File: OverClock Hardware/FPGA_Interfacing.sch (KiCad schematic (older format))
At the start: 17 parts

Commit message: Completed Schematic and ran ERC
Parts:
- gave numbers to parts that had none: 17
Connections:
- no-connect marks 8 -> 10
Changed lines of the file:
@@
 $EndDescr
 $Comp
-L Maxted_Libs:10M02SCE144 U?
+L Maxted_Libs:10M02SCE144 U3
 U 2 1 5C67791D
 P 4350 3300
-F 0 "U?" H 4425 2678 50  0000 C CNN
+F 0 "U3" H 4425 2678 50  0000 C CNN
 F 1 "10M02SCE144" H 4425 2587 50  0000 C CNN
 F 2 "Maxted Libs:QFP-144_EPAD_20x20_Pitch0.5mm" H 5350 4100 50  0001 C CNN
@@
 +3V
 $Comp
-L Device:R_Small R?
+L Device:R_Small R9
 U 1 1 5C68AD28
 P 5900 3700
-F 0 "R?" H 5959 3746 50  0000 L CNN
+F 0 "R9" H 5959 3746 50  0000 L CNN
 F 1 "1K" H 5959 3655 50  0000 L CNN
 F 2 "" H 5900 3700 50  0001 C CNN
@@
 $EndComp
 $Comp
-L power:GND #PWR?
+L power:GND #PWR08
 U 1 1 5C68ADAE
 P 5900 3800
-F 0 "#PWR?" H 5900 3550 50  0001 C CNN
+F 0 "#PWR08" H 5900 3550 50  0001 C CNN
 F 1 "GND" H 5905 3627 50  0000 C CNN
 F 2 "" H 5900 3800 50  0001 C CNN
@@
 	6150 3150 6150 3600
 $Comp
-L Device:R_Small R?
+L Device:R_Small R10
 U 1 1 5C692EE8
 P 6150 3700
-F 0 "R?" H 6209 3746 50  0000 L CNN
+F 0 "R10" H 6209 3746 50  0000 L CNN
 F 1 "1K" H 6209 3655 50  0000 L CNN
 F 2 "" H 6150 3700 50  0001 C CNN
@@
 $EndComp
 $Comp
-L power:GND #PWR?
+L power:GND #PWR09
 U 1 1 5C692FE7
 P 6150 3800
-F 0 "#PWR?" H 6150 3550 50  0001 C CNN
+F 0 "#PWR09" H 6150 3550 50  0001 C CNN
 F 1 "GND" H 6155 3627 50  0000 C CNN
 F 2 "" H 6150 3800 50  0001 C CNN
@@
 	6000 3250 6000 2900
 $Comp
-L Device:R_Small R?
+L Device:R_Small R3
 U 1 1 5C69923E
 P 6000 2800
-F 0 "R?" H 6059 2846 50  0000 L CNN
+F 0 "R3" H 6059 2846 50  0000 L CNN
 F 1 "1K" H 6059 2755 50  0000 L CNN
 F 2 "" H 6000 2800 50  0001 C CNN
@@
 $EndComp
 $Comp
-L Device:R_Small R?
+L Device:R_Small R4
 U 1 1 5C699292
 P 6300 2800
-F 0 "R?" H 6359 2846 50  0000 L CNN
+F 0 "R4" H 6359 2846 50  0000 L CNN
 F 1 "1K" H 6359 2755 50  0000 L CNN
 F 2 "" H 6300 2800 50  0001 C CNN
@@
 Connection ~ 6000 2700
 $Comp
-L Maxted_Libs:JTAG_HDR J?
+L Maxted_Libs:JTAG_HDR J2
 U 1 1 5C6A069B
 P 6700 3300
-F 0 "J?" H 6900 3650 50  0000 L CNN
+F 0 "J2" H 6900 3650 50  0000 L CNN
 F 1 "JTAG_HDR" H 6900 3500 50  0000 L CNN
 F 2 "Connector_PinHeader_2.54mm:PinHeader_2x05_P2.54mm_Vertical" H 6550 4200 50  0001 C CNN
@@
 $EndComp
 $Comp
-L power:GND #PWR?
+L power:GND #PWR07
 U 1 1 5C6A0707
 P 6850 3750
-F 0 "#PWR?" H 6850 3500 50  0001 C CNN
+F 0 "#PWR07" H 6850 3500 50  0001 C CNN
 F 1 "GND" H 6855 3577 50  0000 C CNN
 F 2 "" H 6850 3750 50  0001 C CNN
@@
 	7050 3700 7050 3200
 $Comp
-L Device:C_Small C?
+L Device:C_Small C23
 U 1 1 5C6B33C4
 P 5350 2550
-F 0 "C?" H 5442 2596 50  0000 L CNN
+F 0 "C23" H 5442 2596 50  0000 L CNN
 F 1 "10nF" H 5442 2505 50  0000 L CNN
 F 2 "" H 5350 2550 50  0001 C CNN
@@
 $EndComp
 $Comp
-L power:GND #PWR?
+L power:GND #PWR06
 U 1 1 5C6B34AA
 P 5700 2650
-F 0 "#PWR?" H 5700 2400 50  0001 C CNN
+F 0 "#PWR06" H 5700 2400 50  0001 C CNN
 F 1 "GND" H 5705 2477 50  0000 C CNN
 F 2 "" H 5700 2650 50  0001 C CNN
@@
 	5350 3150 6150 3150
 $Comp
-L Device:C_Small C?
+L Device:C_Small C24
 U 1 1 5C6CAB44
 P 5700 2550
-F 0 "C?" H 5792 2596 50  0000 L CNN
+F 0 "C24" H 5792 2596 50  0000 L CNN
 F 1 "10nF" H 5792 2505 50  0000 L CNN
 F 2 "" H 5700 2550 50  0001 C CNN
@@
 One decoupling cap per Vcc_IO pin.
 $Comp
-L Connector:Conn_01x03_Female J?
+L Connector:Conn_01x03_Female J3
 U 1 1 5C9FC99B
 P 6600 4850
-F 0 "J?" H 6627 4876 50  0000 L CNN
+F 0 "J3" H 6627 4876 50  0000 L CNN
 F 1 "Conn_01x03_Female" H 6300 5100 50  0000 L CNN
 F 2 "Connector_Harwin:Harwin_M20-89003xx_1x03_P2.54mm_Horizontal" H 6600 4850 50  0001 C CNN
@@
 $EndComp
 $Comp
-L power:GND #PWR?
+L power:GND #PWR010
 U 1 1 5C9FCB4B
 P 6400 4950
-F 0 "#PWR?" H 6400 4700 50  0001 C CNN
+F 0 "#PWR010" H 6400 4700 50  0001 C CNN
 F 1 "GND" H 6405 4777 50  0000 C CNN
 F 2 "" H 6400 4950 50  0001 C CNN
@@
 NoConn ~ 5350 3450
 $Comp
-L Maxted_Libs:Switch_Momentary SW?
+L Maxted_Libs:Switch_Momentary SW1
 U 1 1 5CA00362
 P 1850 5100
-F 0 "SW?" H 1800 5250 50  0000 L CNN
+F 0 "SW1" H 1800 5250 50  0000 L CNN
 F 1 "Switch_Momentary" H 1750 5250 50  0001 L CNN
 F 2 "Maxted Libs:Switch_Momentary" H 1600 4950 50  0001 C CNN
@@
 $EndComp
 $Comp
-L Maxted_Libs:Switch_Momentary SW?
+L Maxted_Libs:Switch_Momentary SW2
 U 1 1 5CA005C3
 P 2300 5100
-F 0 "SW?" H 2250 5250 50  0000 L CNN
+F 0 "SW2" H 2250 5250 50  0000 L CNN
 F 1 "Switch_Momentary" H 2200 5250 50  0001 L CNN
 F 2 "Maxted Libs:Switch_Momentary" H 2050 4950 50  0001 C CNN
@@
 $EndComp
 $Comp
-L Maxted_Libs:Switch_Momentary SW?
+L Maxted_Libs:Switch_Momentary SW3
 U 1 1 5CA009D6
 P 2750 5100
-F 0 "SW?" H 2700 5250 50  0000 L CNN
+F 0 "SW3" H 2700 5250 50  0000 L CNN
 F 1 "Switch_Momentary" H 2650 5250 50  0001 L CNN
 F 2 "Maxted Libs:Switch_Momentary" H 2500 4950 50  0001 C CNN
@@
 $EndComp
 $Comp
-L Maxted_Libs:Switch_Momentary SW?
+L Maxted_Libs:Switch_Momentary SW4
 U 1 1 5CA00DE5
 P 3150 5100
-F 0 "SW?" H 3100 5250 50  0000 L CNN
+F 0 "SW4" H 3100 5250 50  0000 L CNN
 F 1 "Switch_Momentary" H 3050 5250 50  0001 L CNN
 F 2 "Maxted Libs:Switch_Momentary" H 2900 4950 50  0001 C CNN
@@
 	3050 5200 2900 5200
 $Comp
-L power:GND #PWR?
+L power:GND #PWR011
 U 1 1 5CA05B6C
 P 1750 5200
-F 0 "#PWR?" H 1750 4950 50  0001 C CNN
+F 0 "#PWR011" H 1750 4950 50  0001 C CNN
 F 1 "GND" H 1755 5027 50  0000 C CNN
 F 2 "" H 1750 5200 50  0001 C CNN
@@
 	1700 5750 1700 5450
 $Comp
-L Device:R_Small R?
+L Device:R_Small R8
 U 1 1 5CA06FA7
 P 3150 3100
-F 0 "R?" H 3209 3146 50  0000 L CNN
+F 0 "R8" H 3209 3146 50  0000 L CNN
 F 1 "1K" H 3209 3055 50  0000 L CNN
 F 2 "Resistor_SMD:R_0805_2012Metric_Pad1.15x1.40mm_HandSolder" H 3150 3100 50  0001 C CNN
@@
 $EndComp
 $Comp
-L Device:R_Small R?
+L Device:R_Small R7
 U 1 1 5CA0718A
 P 2750 3100
-F 0 "R?" H 2809 3146 50  0000 L CNN
+F 0 "R7" H 2809 3146 50  0000 L CNN
 F 1 "1K" H 2809 3055 50  0000 L CNN
 F 2 "Resistor_SMD:R_0805_2012Metric_Pad1.15x1.40mm_HandSolder" H 2750 3100 50  0001 C CNN
@@
 $EndComp
 $Comp
-L Device:R_Small R?
+L Device:R_Small R6
 U 1 1 5CA081C0
 P 2300 3100
-F 0 "R?" H 2359 3146 50  0000 L CNN
+F 0 "R6" H 2359 3146 50  0000 L CNN
 F 1 "1K" H 2359 3055 50  0000 L CNN
 F 2 "Resistor_SMD:R_0805_2012Metric_Pad1.15x1.40mm_HandSolder" H 2300 3100 50  0001 C CNN
@@
 $EndComp
 $Comp
-L Device:R_Small R?
+L Device:R_Small R5
 U 1 1 5CA09200
 P 1850 3100
-F 0 "R?" H 1909 3146 50  0000 L CNN
+F 0 "R5" H 1909 3146 50  0000 L CNN
 F 1 "1K" H 1909 3055 50  0000 L CNN
 F 2 "Resistor_SMD:R_0805_2012Metric_Pad1.15x1.40mm_HandSolder" H 1850 3100 50  0001 C CNN
@@
 NoConn ~ 3500 3150
 NoConn ~ 3500 3250
+NoConn ~ 5350 2850
+NoConn ~ 5350 2950
 $EndSCHEMATC

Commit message: Matched symbols to footprints and generated netlist
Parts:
- C23, C24: footprint (none) -> Capacitor_SMD:C_0805_2012Metric_Pad1.15x1.40mm_HandSolder
- R10, R3, R4, R9: footprint (none) -> Resistor_SMD:R_0805_2012Metric_Pad1.15x1.40mm_HandSolder
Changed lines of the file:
@@
 F 0 "R9" H 5959 3746 50  0000 L CNN
 F 1 "1K" H 5959 3655 50  0000 L CNN
-F 2 "" H 5900 3700 50  0001 C CNN
+F 2 "Resistor_SMD:R_0805_2012Metric_Pad1.15x1.40mm_HandSolder" H 5900 3700 50  0001 C CNN
 F 3 "~" H 5900 3700 50  0001 C CNN
 	1    5900 3700
@@
 F 0 "R10" H 6209 3746 50  0000 L CNN
 F 1 "1K" H 6209 3655 50  0000 L CNN
-F 2 "" H 6150 3700 50  0001 C CNN
+F 2 "Resistor_SMD:R_0805_2012Metric_Pad1.15x1.40mm_HandSolder" H 6150 3700 50  0001 C CNN
 F 3 "~" H 6150 3700 50  0001 C CNN
 	1    6150 3700
@@
 F 0 "R3" H 6059 2846 50  0000 L CNN
 F 1 "1K" H 6059 2755 50  0000 L CNN
-F 2 "" H 6000 2800 50  0001 C CNN
+F 2 "Resistor_SMD:R_0805_2012Metric_Pad1.15x1.40mm_HandSolder" H 6000 2800 50  0001 C CNN
 F 3 "~" H 6000 2800 50  0001 C CNN
 	1    6000 2800
@@
 F 0 "R4" H 6359 2846 50  0000 L CNN
 F 1 "1K" H 6359 2755 50  0000 L CNN
-F 2 "" H 6300 2800 50  0001 C CNN
+F 2 "Resistor_SMD:R_0805_2012Metric_Pad1.15x1.40mm_HandSolder" H 6300 2800 50  0001 C CNN
 F 3 "~" H 6300 2800 50  0001 C CNN
 	1    6300 2800
@@
 F 0 "C23" H 5442 2596 50  0000 L CNN
 F 1 "10nF" H 5442 2505 50  0000 L CNN
-F 2 "" H 5350 2550 50  0001 C CNN
+F 2 "Capacitor_SMD:C_0805_2012Metric_Pad1.15x1.40mm_HandSolder" H 5350 2550 50  0001 C CNN
 F 3 "~" H 5350 2550 50  0001 C CNN
 	1    5350 2550
@@
 F 0 "C24" H 5792 2596 50  0000 L CNN
 F 1 "10nF" H 5792 2505 50  0000 L CNN
-F 2 "" H 5700 2550 50  0001 C CNN
+F 2 "Capacitor_SMD:C_0805_2012Metric_Pad1.15x1.40mm_HandSolder" H 5700 2550 50  0001 C CNN
 F 3 "~" H 5700 2550 50  0001 C CNN
 	1    5700 2550

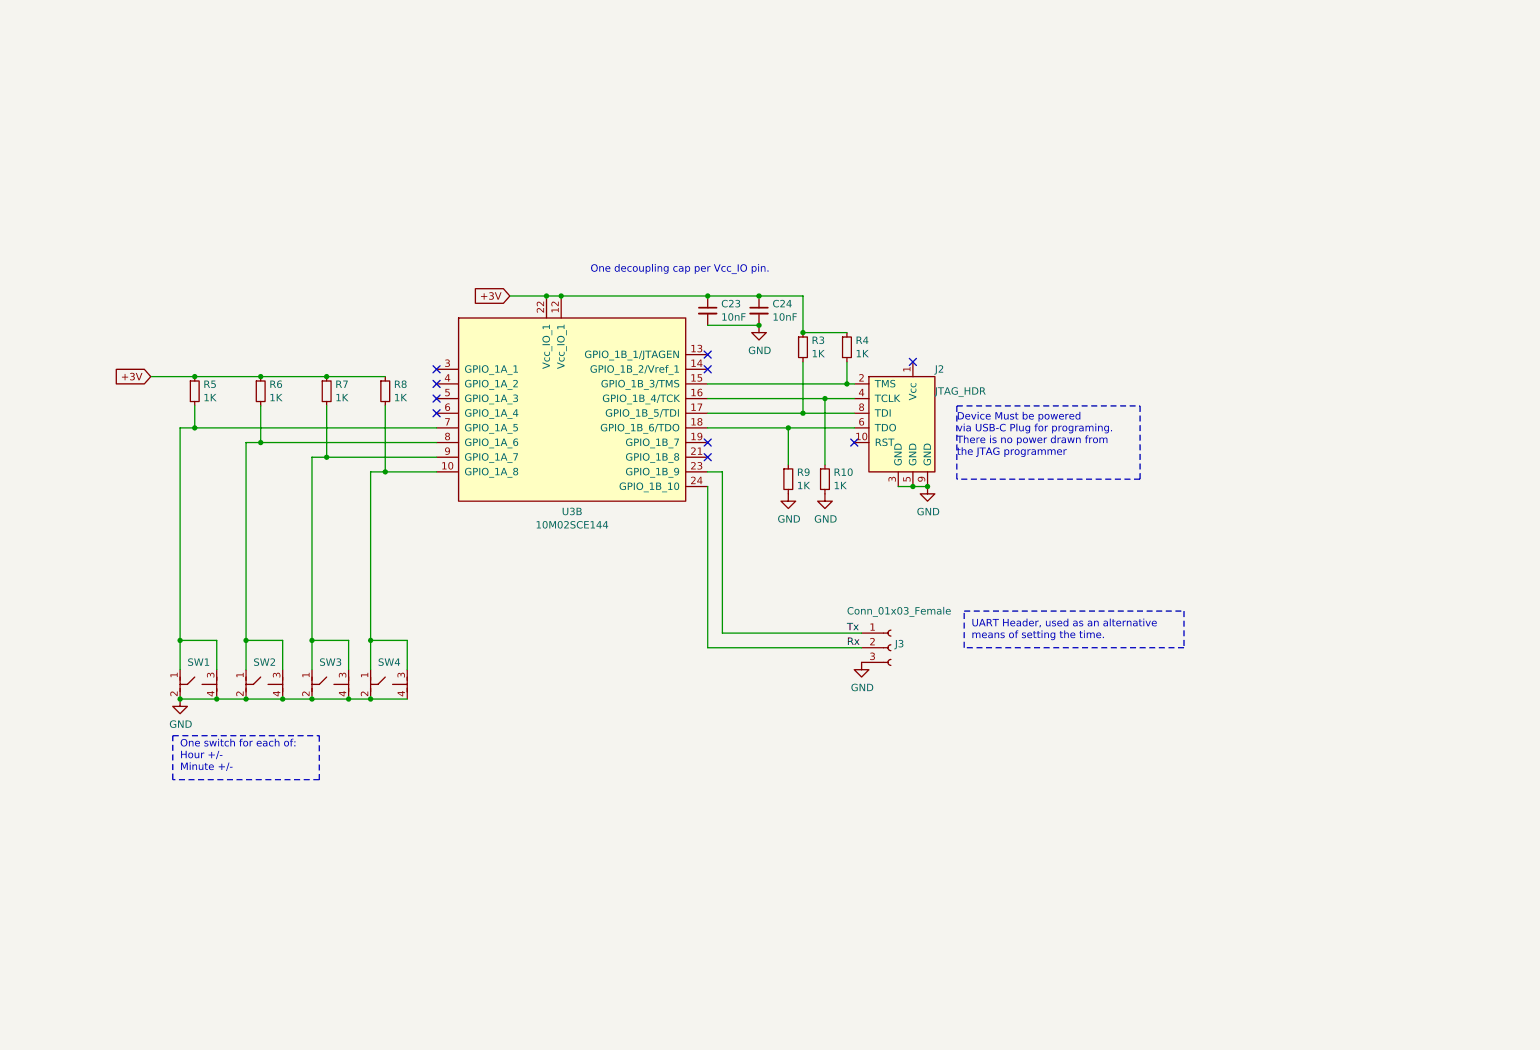
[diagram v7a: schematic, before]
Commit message: Place and route Decoupling Capacitors
Placed and routed all the decoupling capacitors for the FPGA. Created Top and bottom GND planes too for better signal integrity
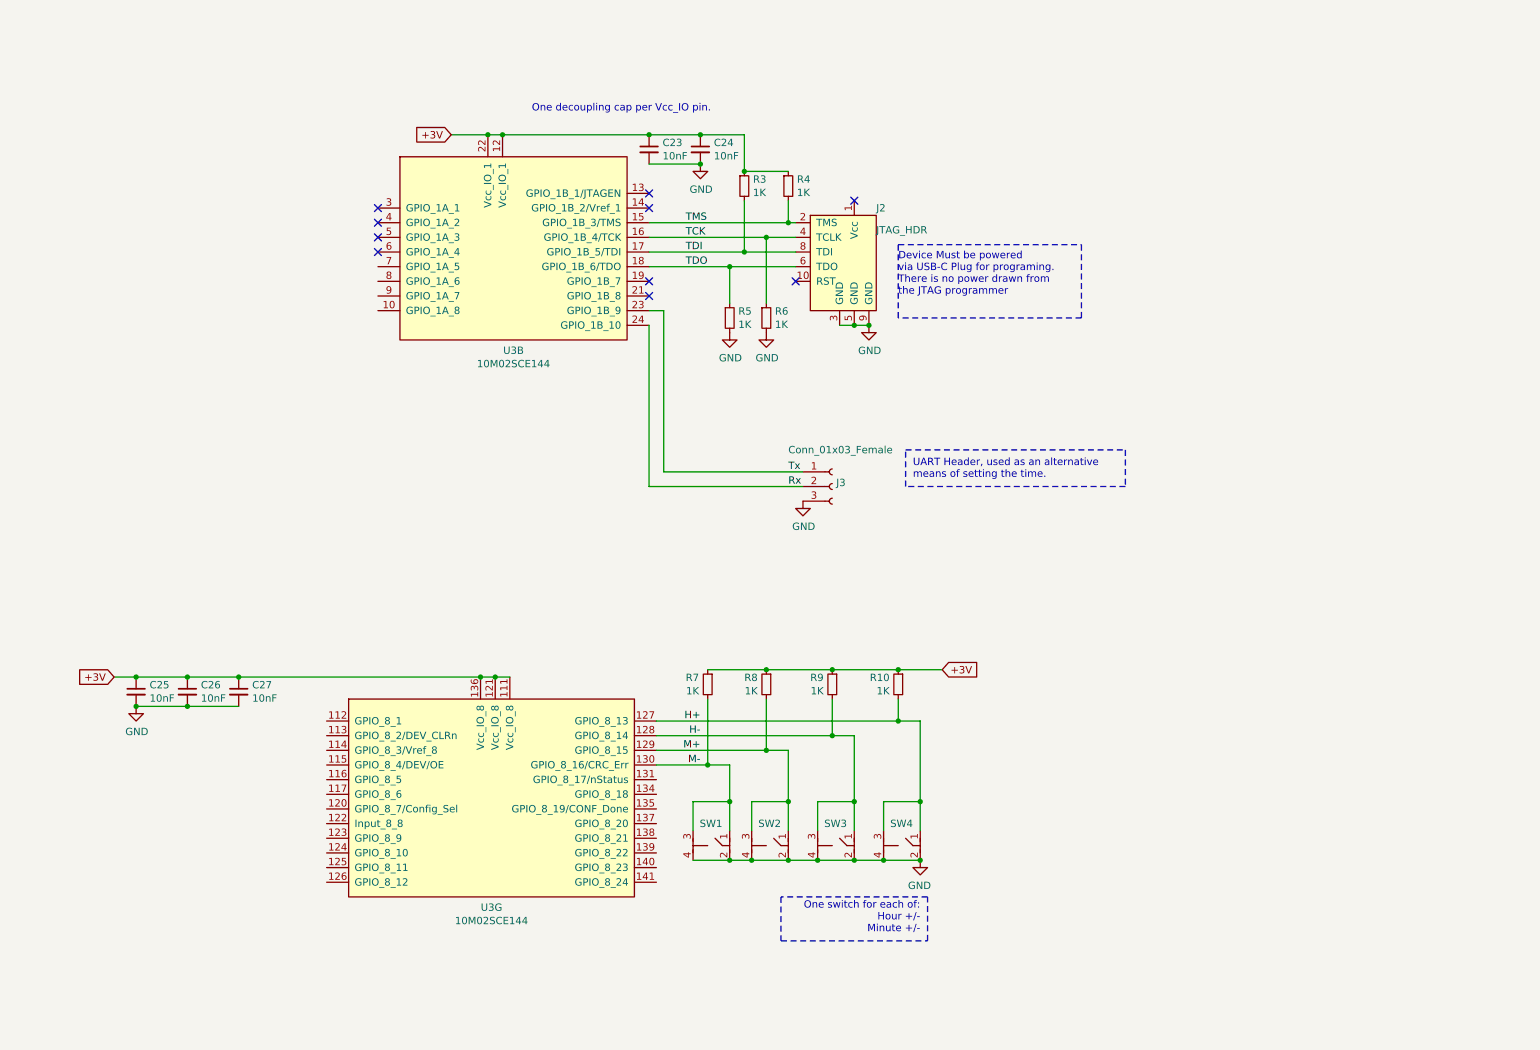
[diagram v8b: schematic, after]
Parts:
- added C25, C26, C27: 10nF, Capacitor_SMD:C_0603_1608Metric_Pad1.05x0.95mm_HandSolder, symbol Device:C_Small
- added unit 7 of U3
- C23, C24: footprint Capacitor_SMD:C_0805_2012Metric_Pad1.15x1.40mm_HandSolder -> Capacitor_SMD:C_0603_1608Metric_Pad1.05x0.95mm_HandSolder
- renumbered R5 to R10, R9 to R5, R10 to R6, R8 to R7, R7 to R8, R6 to R9, SW4 to SW1, SW3 to SW2, SW2 to SW3, SW1 to SW4
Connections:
- net +3V: now also C25.1, C26.1, C27.1, U3.111 (Vcc_IO_8), U3.121 (Vcc_IO_8), U3.136 (Vcc_IO_8)
- net GND: now also C25.2, C26.2, C27.2
- net M-: now reaches R7.2, SW1.1, SW1.3
- net M-: now also U3.130 (GPIO_8_16/CRC_Err); no longer U3.10 (GPIO_1A_8)
- net TMS: now reaches J2.2 (TMS), R4.2, U3.15 (GPIO_1B_3/TMS)
- net TCK: now reaches J2.4 (TCLK), R6.1, U3.16 (GPIO_1B_4/TCK)
- net TDI: now reaches J2.8 (TDI), R3.2, U3.17 (GPIO_1B_5/TDI)
- net TDO: now reaches J2.6 (TDO), R5.1, U3.18 (GPIO_1B_6/TDO)
- net H+: now reaches R10.2, SW4.1, SW4.3
- net H+: now also U3.127 (GPIO_8_13); no longer U3.7 (GPIO_1A_5)
- net H-: now reaches R9.2, SW3.1, SW3.3
- net H-: now also U3.128 (GPIO_8_14); no longer U3.8 (GPIO_1A_6)
- net M+: now reaches R8.2, SW2.1, SW2.3
- net M+: now also U3.129 (GPIO_8_15); no longer U3.9 (GPIO_1A_7)
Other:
- moved on the sheet: C23, C24, J2, J3, R10, R3, R4, R5, R6, R7, R8, R9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
